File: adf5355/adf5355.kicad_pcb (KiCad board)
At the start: 4 copper layers, 48.3 x 48.3 mm, 102 parts, among them J1 REF_IN_A, J2 RF_B, J3 RF_A_P, J4 REF_IN_B, J5 RF_A_N, J6 Conn_01x02_Male, J7 Conn_01x10_Male, U1 L7806, U2 ADM7150, U3 ADM7150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

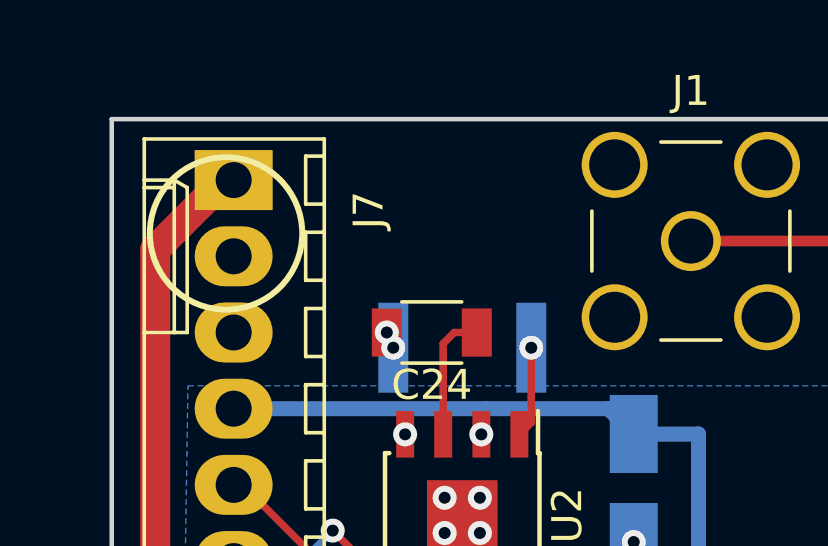
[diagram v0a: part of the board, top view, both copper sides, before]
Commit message: Added layer markings
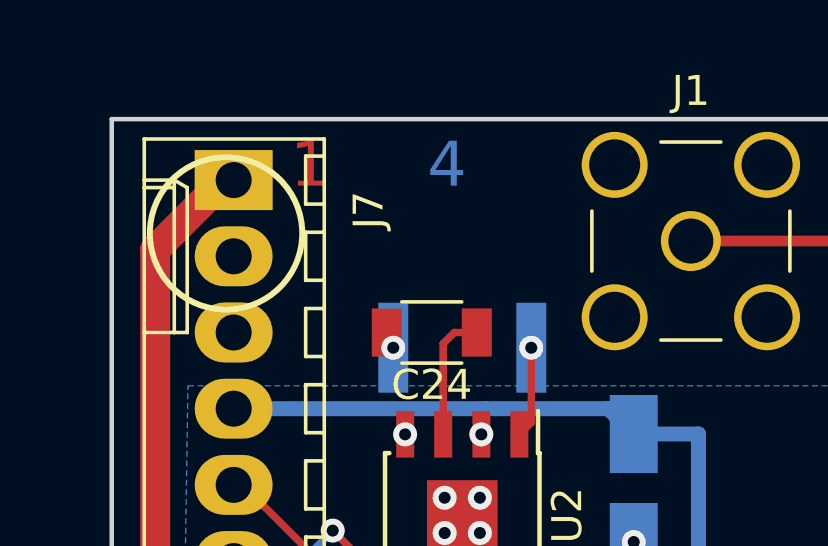
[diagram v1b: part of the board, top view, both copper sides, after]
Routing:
- net GND: vias 69 -> 68
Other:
- board text added: "1"
- board text added: "2"
- board text added: "3"
- board text added: "4"
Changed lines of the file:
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@@
   (general
     (thickness 1.6)
-    (drawings 14)
-    (tracks 823)
+    (drawings 18)
+    (tracks 822)
     (zones 0)
     (modules 102)
@@
     (2 In2.Cu signal)
     (31 B.Cu signal)
-    (32 B.Adhes user)
-    (33 F.Adhes user)
+    (32 B.Adhes user hide)
+    (33 F.Adhes user hide)
     (34 B.Paste user hide)
-    (35 F.Paste user)
+    (35 F.Paste user hide)
     (36 B.SilkS user hide)
-    (37 F.SilkS user)
+    (37 F.SilkS user hide)
     (38 B.Mask user hide)
     (39 F.Mask user hide)
-    (40 Dwgs.User user)
+    (40 Dwgs.User user hide)
     (41 Cmts.User user hide)
-    (42 Eco1.User user)
-    (43 Eco2.User user)
+    (42 Eco1.User user hide)
+    (43 Eco2.User user hide)
     (44 Edge.Cuts user)
     (45 Margin user hide)
@@
     (visible_elements FFFFF77F)
     (pcbplotparams
-      (layerselection 0x3d0f0_ffffffff)
+      (layerselection 0x010f0_ffffffff)
       (usegerberextensions false)
       (usegerberattributes false)
@@
       (padsonsilk false)
       (subtractmaskfromsilk false)
-      (outputformat 4)
+      (outputformat 1)
       (mirror false)
       (drillshape 0)
       (scaleselection 1)
-      (outputdirectory ""))
+      (outputdirectory "gerber/"))
   )
   (net 0 "")
@@
     )
   )
+  (gr_text 4 (at 94.996 80.264) (layer B.Cu)
+    (effects (font (size 1.5 1.5) (thickness 0.3)))
+  )
+  (gr_text 3 (at 93.472 80.264) (layer In2.Cu)
+    (effects (font (size 1.5 1.5) (thickness 0.3)))
+  )
+  (gr_text 2 (at 91.948 80.264) (layer In1.Cu)
+    (effects (font (size 1.5 1.5) (thickness 0.3)))
+  )
+  (gr_text 1 (at 90.424 80.264) (layer F.Cu)
+    (effects (font (size 1.5 1.5) (thickness 0.3)))
+  )
   (gr_text "3V3 REG\nHERE" (at 124.46 91.44 90) (layer F.SilkS)
     (effects (font (size 1.5 1.5) (thickness 0.3)))
@@
   (via (at 96.0915 92.5355) (size 0.8) (drill 0.4) (layers F.Cu B.Cu) (net 2))
   (via (at 93.599 89.248) (size 0.8) (drill 0.4) (layers F.Cu B.Cu) (net 2))
-  (via (at 92.988 85.852) (size 0.8) (drill 0.4) (layers F.Cu B.Cu) (net 2))
   (via (at 93.204 86.36) (size 0.8) (drill 0.4) (layers F.Cu B.Cu) (net 2))
   (via (at 101.219 92.837) (size 0.8) (drill 0.4) (layers F.Cu B.Cu) (net 2))
@@
   (segment (start 110.19663 83.566) (end 110.17114 83.59149) (width 0.254) (layer F.Cu) (net 45))
   (segment (start 111.638 83.566) (end 110.19663 83.566) (width 0.254) (layer F.Cu) (net 45))
-  (segment (start 108.67114 82.96249) (end 108.67114 83.59149) (width 0.355) (layer F.Cu) (net 46) (status 1000000))
-  (segment (start 103.124 82.804) (end 108.51265 82.804) (width 0.355) (layer F.Cu) (net 46) (status 1000000))
-  (segment (start 108.51265 82.804) (end 108.67114 82.96249) (width 0.355) (layer F.Cu) (net 46) (status 1000000))
+  (segment (start 108.67114 82.96249) (end 108.67114 83.59149) (width 0.355) (layer F.Cu) (net 46))
+  (segment (start 103.124 82.804) (end 108.51265 82.804) (width 0.355) (layer F.Cu) (net 46))
+  (segment (start 108.51265 82.804) (end 108.67114 82.96249) (width 0.355) (layer F.Cu) (net 46))
   (segment (start 112.141 87.317001) (end 112.141 88.779382) (width 0.254) (layer F.Cu) (net 47))
   (segment (start 112.014 86.59) (end 112.014 87.190001) (width 0.254) (layer F.Cu) (net 47))
@@
     (polygon
       (pts
-        (xy 83.82 78.74) (xy 132.08 78.74) (xy 132.08 127) (xy 83.82 127)
+        (xy 83.82 78.74) (xy 89.408 78.74) (xy 89.408 81.788) (xy 96.012 81.788) (xy 96.012 78.74)
+        (xy 132.08 78.74) (xy 132.08 127) (xy 83.82 127)
       )
     )

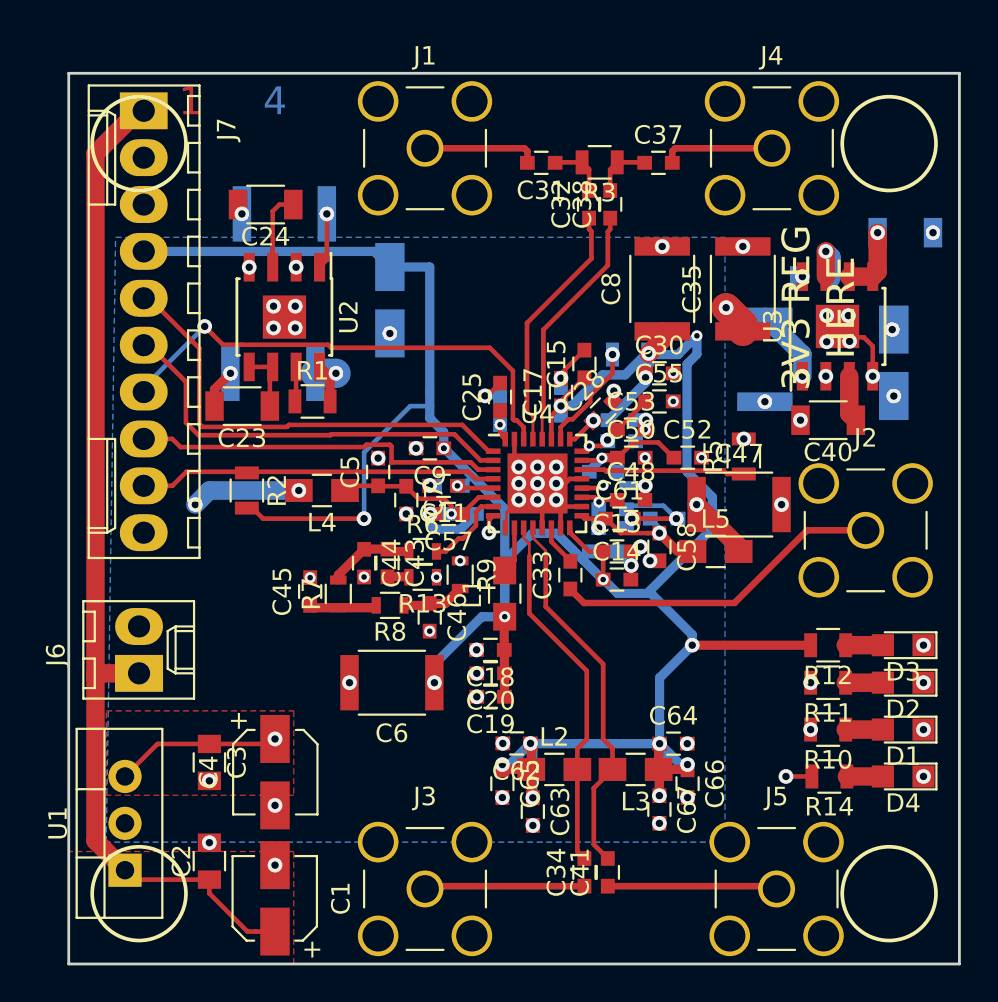
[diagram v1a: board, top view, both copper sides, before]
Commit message: Found via that caused DRC error at manufacturer
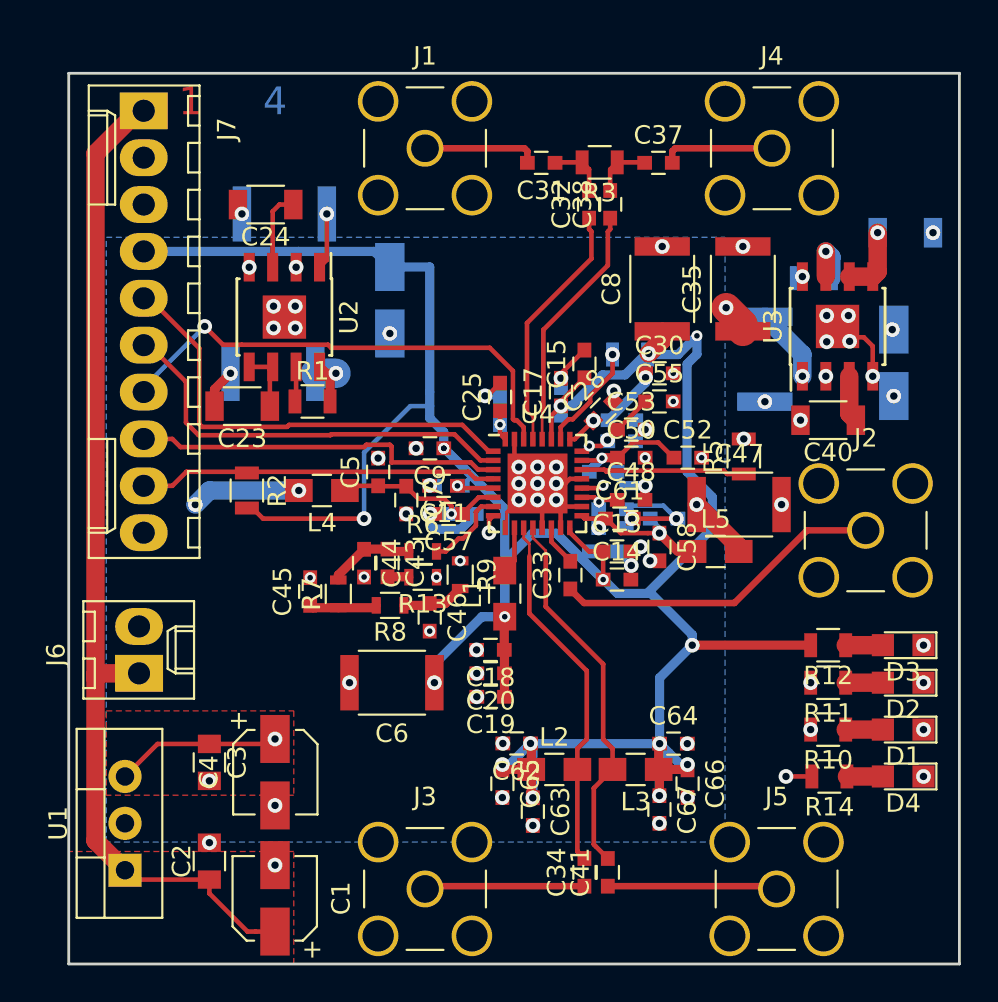
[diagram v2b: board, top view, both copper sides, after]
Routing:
- net GND: track 383.7 -> 383.9 mm, vias 68 -> 67
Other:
- board text removed: "3V3 REG HERE"
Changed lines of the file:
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@@
   (general
     (thickness 1.6)
-    (drawings 18)
-    (tracks 822)
+    (drawings 8)
+    (tracks 820)
     (zones 0)
     (modules 102)
@@
   (page A4)
   (layers
-    (0 F.Cu signal)
-    (1 In1.Cu signal)
-    (2 In2.Cu signal)
-    (31 B.Cu signal)
+    (0 F.Cu signal hide)
+    (1 In1.Cu signal hide)
+    (2 In2.Cu signal hide)
+    (31 B.Cu signal hide)
     (32 B.Adhes user hide)
     (33 F.Adhes user hide)
     (34 B.Paste user hide)
     (35 F.Paste user hide)
-    (36 B.SilkS user hide)
+    (36 B.SilkS user)
     (37 F.SilkS user hide)
     (38 B.Mask user hide)
@@
     (effects (font (size 1.5 1.5) (thickness 0.3)))
   )
-  (gr_text "3V3 REG\nHERE" (at 124.46 91.44 90) (layer F.SilkS)
-    (effects (font (size 1.5 1.5) (thickness 0.3)))
-  )
-  (gr_circle (center 87.63 123.19) (end 87.63 120.65) (layer F.SilkS) (width 0.2))
-  (gr_circle (center 128.27 123.19) (end 128.27 120.65) (layer F.SilkS) (width 0.2))
-  (gr_circle (center 128.27 82.55) (end 128.27 80.01) (layer F.SilkS) (width 0.2))
-  (gr_circle (center 87.63 82.55) (end 87.63 80.01) (layer F.SilkS) (width 0.2))
-  (dimension 19.05 (width 0.3) (layer F.SilkS)
-    (gr_text "19,050 mm" (at 144.339999 112.395 270) (layer F.SilkS)
-      (effects (font (size 1.5 1.5) (thickness 0.3)))
-    )
-    (feature1 (pts (xy 135.89 121.92) (xy 142.82642 121.92)))
-    (feature2 (pts (xy 135.89 102.87) (xy 142.82642 102.87)))
-    (crossbar (pts (xy 142.239999 102.87) (xy 142.239999 121.92)))
-    (arrow1a (pts (xy 142.239999 121.92) (xy 141.653578 120.793496)))
-    (arrow1b (pts (xy 142.239999 121.92) (xy 142.82642 120.793496)))
-    (arrow2a (pts (xy 142.239999 102.87) (xy 141.653578 103.996504)))
-    (arrow2b (pts (xy 142.239999 102.87) (xy 142.82642 103.996504)))
-  )
-  (dimension 19.05 (width 0.3) (layer F.SilkS)
-    (gr_text "19,050 mm" (at 144.34 93.345 270) (layer F.SilkS)
-      (effects (font (size 1.5 1.5) (thickness 0.3)))
-    )
-    (feature1 (pts (xy 135.89 102.87) (xy 142.826421 102.87)))
-    (feature2 (pts (xy 135.89 83.82) (xy 142.826421 83.82)))
-    (crossbar (pts (xy 142.24 83.82) (xy 142.24 102.87)))
-    (arrow1a (pts (xy 142.24 102.87) (xy 141.653579 101.743496)))
-    (arrow1b (pts (xy 142.24 102.87) (xy 142.826421 101.743496)))
-    (arrow2a (pts (xy 142.24 83.82) (xy 141.653579 84.946504)))
-    (arrow2b (pts (xy 142.24 83.82) (xy 142.826421 84.946504)))
-  )
-  (dimension 19.05 (width 0.3) (layer F.SilkS)
-    (gr_text "19,050 mm" (at 108.585 66.48) (layer F.SilkS)
-      (effects (font (size 1.5 1.5) (thickness 0.3)))
-    )
-    (feature1 (pts (xy 118.11 76.2) (xy 118.11 67.993579)))
-    (feature2 (pts (xy 99.06 76.2) (xy 99.06 67.993579)))
-    (crossbar (pts (xy 99.06 68.58) (xy 118.11 68.58)))
-    (arrow1a (pts (xy 118.11 68.58) (xy 116.983496 69.166421)))
-    (arrow1b (pts (xy 118.11 68.58) (xy 116.983496 67.993579)))
-    (arrow2a (pts (xy 99.06 68.58) (xy 100.186504 69.166421)))
-    (arrow2b (pts (xy 99.06 68.58) (xy 100.186504 67.993579)))
-  )
   (gr_line (start 132.08 78.74) (end 83.82 78.74) (layer Edge.Cuts) (width 0.15))
   (gr_line (start 132.08 127) (end 132.08 78.74) (layer Edge.Cuts) (width 0.15))
   (gr_line (start 83.82 127) (end 132.08 127) (layer Edge.Cuts) (width 0.15))
   (gr_line (start 83.82 78.74) (end 83.82 127) (layer Edge.Cuts) (width 0.15))
-  (dimension 48.26 (width 0.3) (layer F.SilkS)
-    (gr_text "48,260 mm" (at 107.95 136.72) (layer F.SilkS)
-      (effects (font (size 1.5 1.5) (thickness 0.3)))
-    )
-    (feature1 (pts (xy 132.08 127) (xy 132.08 135.206421)))
-    (feature2 (pts (xy 83.82 127) (xy 83.82 135.206421)))
-    (crossbar (pts (xy 83.82 134.62) (xy 132.08 134.62)))
-    (arrow1a (pts (xy 132.08 134.62) (xy 130.953496 135.206421)))
-    (arrow1b (pts (xy 132.08 134.62) (xy 130.953496 134.033579)))
-    (arrow2a (pts (xy 83.82 134.62) (xy 84.946504 135.206421)))
-    (arrow2b (pts (xy 83.82 134.62) (xy 84.946504 134.033579)))
-  )
-  (dimension 48.26 (width 0.3) (layer F.SilkS)
-    (gr_text "48,260 mm" (at 76.64 102.87 270) (layer F.SilkS)
-      (effects (font (size 1.5 1.5) (thickness 0.3)))
-    )
-    (feature1 (pts (xy 83.82 127) (xy 78.153579 127)))
-    (feature2 (pts (xy 83.82 78.74) (xy 78.153579 78.74)))
-    (crossbar (pts (xy 78.74 78.74) (xy 78.74 127)))
-    (arrow1a (pts (xy 78.74 127) (xy 78.153579 125.873496)))
-    (arrow1b (pts (xy 78.74 127) (xy 79.326421 125.873496)))
-    (arrow2a (pts (xy 78.74 78.74) (xy 78.153579 79.866504)))
-    (arrow2b (pts (xy 78.74 78.74) (xy 79.326421 79.866504)))
-  )
   (segment (start 87.376 122.428) (end 86.868 121.92) (width 0.25) (layer F.Cu) (net 1))
   (segment (start 91.44 122.428) (end 87.376 122.428) (width 0.25) (layer F.Cu) (net 1))
@@
   (via (at 115.05 99.568) (size 0.6) (drill 0.3) (layers F.Cu B.Cu) (net 2))
   (segment (start 114.3 98.933) (end 114.415 98.933) (width 0.25) (layer B.Cu) (net 2))
-  (via (at 115.05 98.044) (size 0.6) (drill 0.3) (layers F.Cu B.Cu) (net 2))
   (segment (start 115.05 99.568) (end 115.05 98.044) (width 0.25) (layer In1.Cu) (net 2))
   (segment (start 115.093152 98.000848) (end 115.05 98.044) (width 0.25) (layer In1.Cu) (net 2))
@@
   (segment (start 113.526 100.33) (end 113.526 100.690586) (width 0.25) (layer B.Cu) (net 2))
   (segment (start 113.526 100.690586) (end 113.890414 101.055) (width 0.25) (layer B.Cu) (net 2))
-  (via (at 115.093152 97.526154) (size 0.8) (drill 0.4) (layers F.Cu B.Cu) (net 2))
-  (segment (start 114.542 97.536) (end 115.083306 97.536) (width 0.25) (layer B.Cu) (net 2))
-  (segment (start 115.083306 97.536) (end 115.093152 97.526154) (width 0.25) (layer B.Cu) (net 2))
   (via (at 100.584 99.592) (size 0.8) (drill 0.4) (layers F.Cu B.Cu) (net 2))
   (via (at 102.64 99.06) (size 0.8) (drill 0.4) (layers F.Cu B.Cu) (net 2))
@@
   (segment (start 114.808 103.350002) (end 114.327998 102.87) (width 0.25) (layer In1.Cu) (net 2))
   (segment (start 114.808 104.394) (end 114.808 103.350002) (width 0.25) (layer In1.Cu) (net 2))
-  (segment (start 114.53 98.564) (end 115.05 98.044) (width 0.25) (layer B.Cu) (net 2))
-  (segment (start 114.53 98.679) (end 114.53 98.564) (width 0.25) (layer B.Cu) (net 2))
   (segment (start 103.665314 103.441001) (end 103.405998 103.181685) (width 0.5) (layer B.Cu) (net 2))
   (segment (start 103.405998 103.181685) (end 103.405998 102.616) (width 0.5) (layer B.Cu) (net 2))
@@
   (segment (start 109.081 119.38) (end 108.966 119.495) (width 0.5) (layer In1.Cu) (net 2))
   (segment (start 115.824 119.38) (end 109.081 119.38) (width 0.5) (layer In1.Cu) (net 2))
+  (via (at 115.05 98.044) (size 0.8) (drill 0.4) (layers F.Cu B.Cu) (net 2))
+  (segment (start 114.53 98.564) (end 115.05 98.044) (width 0.25) (layer B.Cu) (net 2))
+  (segment (start 114.53 98.679) (end 114.53 98.564) (width 0.25) (layer B.Cu) (net 2))
+  (segment (start 114.542 97.536) (end 115.05 98.044) (width 0.25) (layer B.Cu) (net 2))
   (segment (start 88.63 115.078) (end 86.868 116.84) (width 0.25) (layer F.Cu) (net 3))
   (segment (start 91.44 115.078) (end 88.63 115.078) (width 0.25) (layer F.Cu) (net 3))
@@
     (polygon
       (pts
-        (xy 86.36 87.63) (xy 119.38 87.63) (xy 119.38 120.396) (xy 85.852 120.396)
+        (xy 85.852 87.63) (xy 119.38 87.63) (xy 119.38 120.396) (xy 85.852 120.396)
       )
     )
